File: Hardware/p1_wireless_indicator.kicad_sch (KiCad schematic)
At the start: 41 parts, among them J1 615006138421, J2 629722000214, SW1 KSEM31JLFS, SW2 KSEM31JLFS, U1 140357145100, U2 140357145100, U3 173950336, U4 ESP32-C3-WROOM-02-N4

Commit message: Updated Layout
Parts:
- L1: footprint Inductor_SMD:L_Wuerth_WE-PD2-Typ-MS -> manul_tech:7447730
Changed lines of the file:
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@@
     (title "P1 Wireless Interface")
     (date "2024-03-17")
-    (rev "1.0.0")
+    (rev "1.1.0")
     (company "Manul Technologies")
   )
@@
       (effects (font (size 1.27 1.27)))
     )
-    (property "Footprint" "Inductor_SMD:L_Wuerth_WE-PD2-Typ-MS" (at 45.72 177.165 0)
-      (effects (font (size 1.27 1.27)) hide)
-    )
+    (property "Footprint" "manul_tech:7447730" (at 45.72 177.165 0)
+      (effects (font (size 1.27 1.27)) hide)
+    )

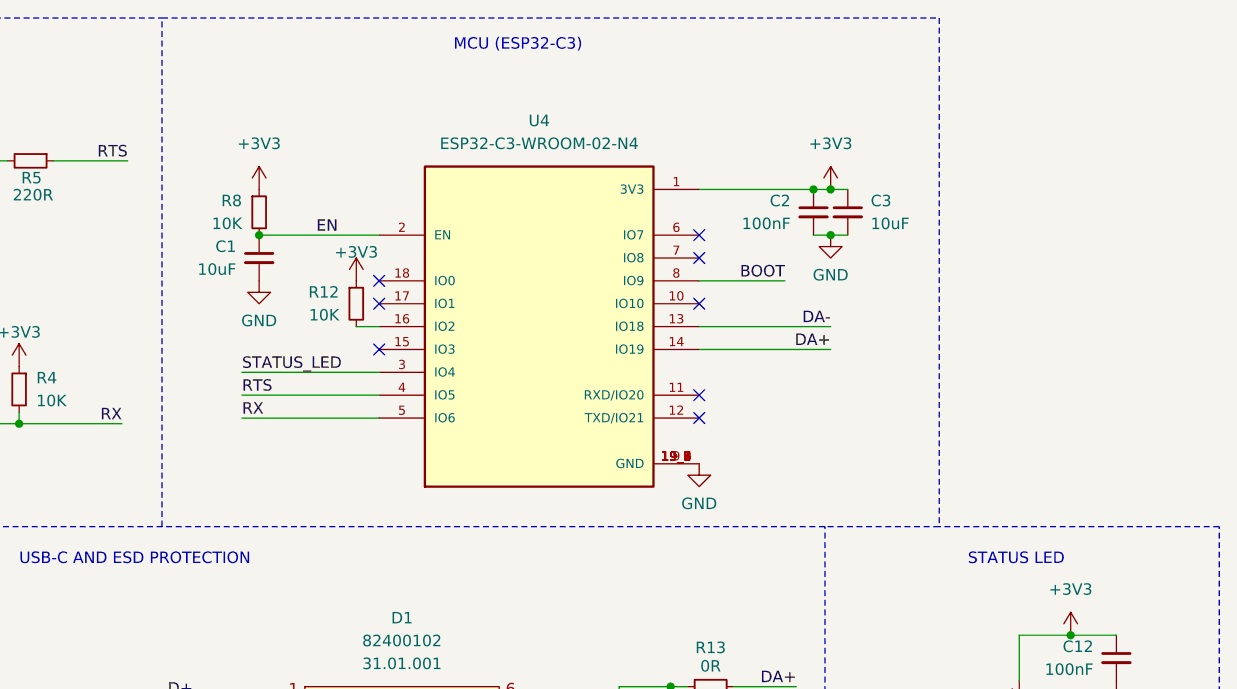
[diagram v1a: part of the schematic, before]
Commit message: Added 10K resistor on GPIO8 to fix boot issue
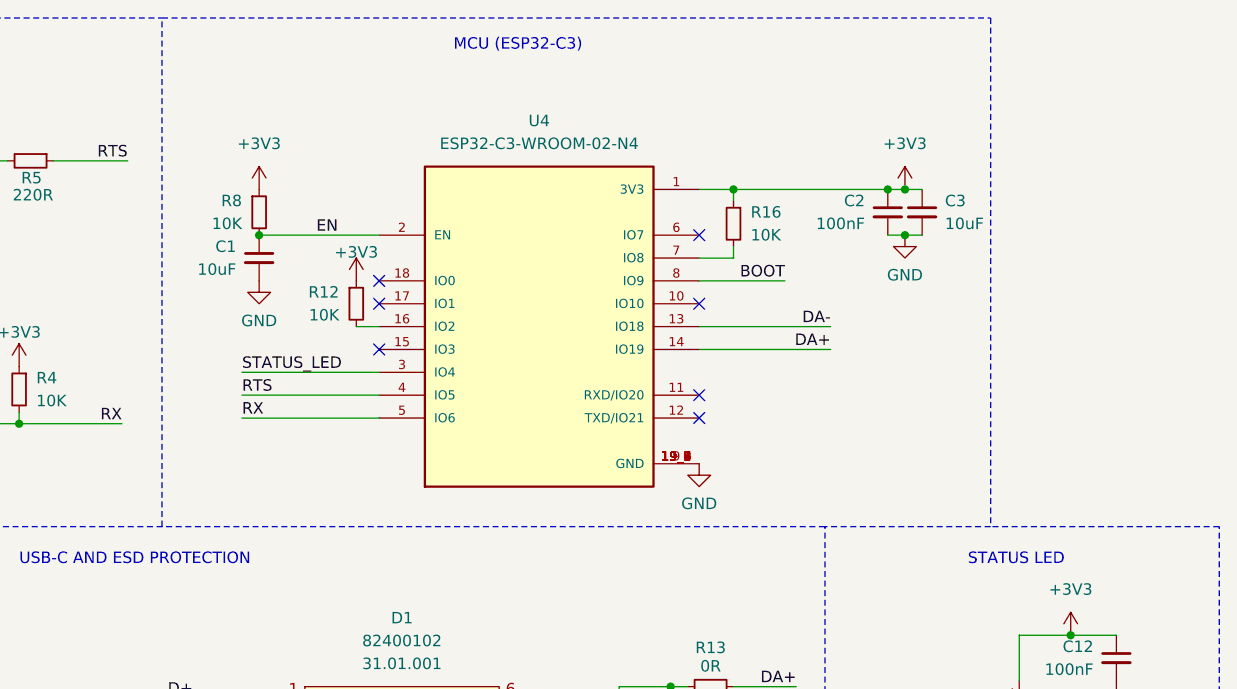
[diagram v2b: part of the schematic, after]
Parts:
- added R16: 10K, Resistor_SMD:R_0402_1005Metric, symbol Device:R_Small
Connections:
- net +3V3: now also R16.1
- net at U4.7 (IO8): now also R16.2
- no-connect marks 14 -> 13
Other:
- moved on the sheet: C2, C3

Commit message: Rounting of V2.0
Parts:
- removed R2: 1M, Resistor_SMD:R_0402_1005Metric, symbol Device:R_Small
- added R17: 1M, Resistor_SMD:R_0402_1005Metric, symbol Device:R_Small
- R3: value 1K -> 220R; MPN CRCW04021K00DHEDP -> CRCW0402220RFKED; internalRef 12.02.026 -> 12.02.008
- U1, U2: footprint Package_SO:SOP-4_3.8x4.1mm_P2.54mm -> manul_tech:140357145100
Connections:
- net GND: now also R17.2; no longer U2.3
- net RX: now also U2.3, R17.1; no longer R4.2, U2.4
- new net: R4.2, U2.4
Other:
- moved on the sheet: C10, C11, D1, D2, D3, R13, R14, R3, R4, U2
